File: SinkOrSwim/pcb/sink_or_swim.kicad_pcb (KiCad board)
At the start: 2 copper layers, 42.7 x 68.1 mm, 23 parts, among them P101 CONN_01X02, P102 CONN_01X03, P103 CONN_01X02, P201 CONN_01X01, Q201 BUK9575-100A, U201 LMV358, U401 LM2931

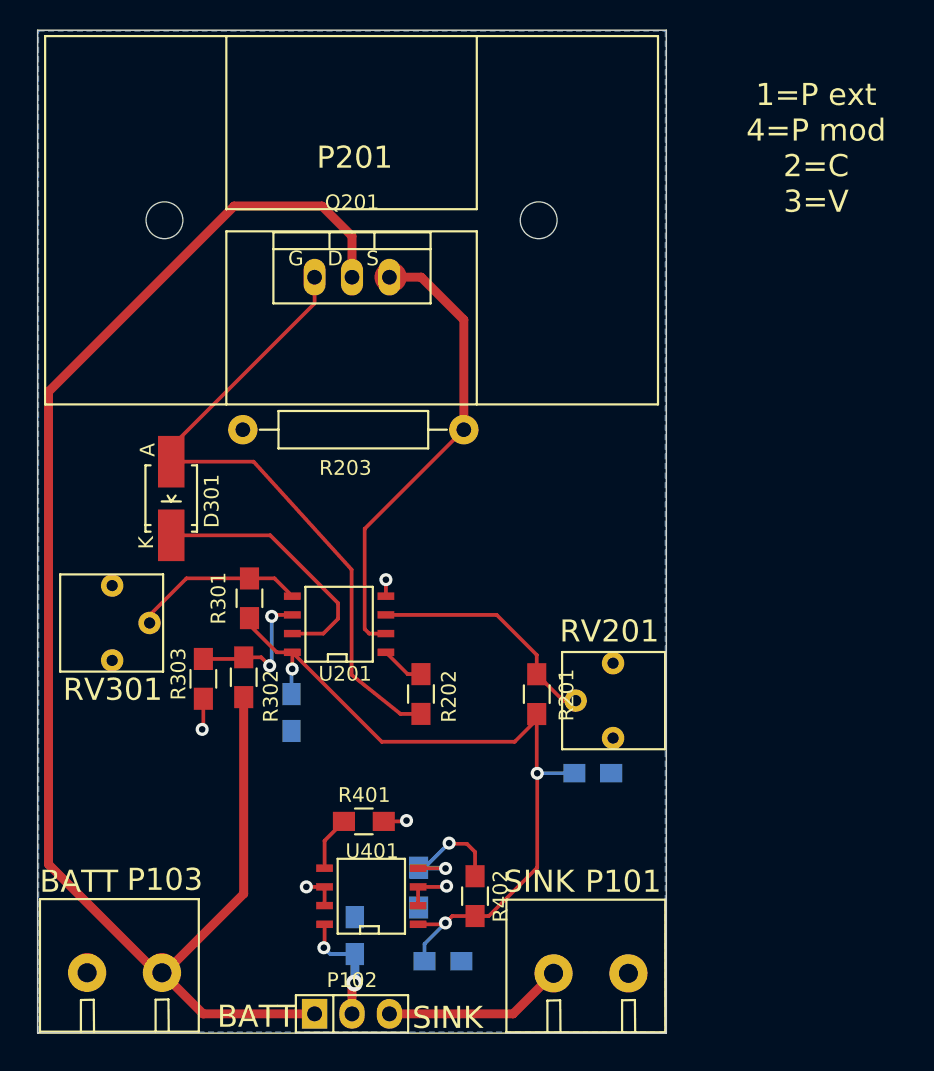
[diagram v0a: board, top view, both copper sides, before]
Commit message: Better Layout.  Added 2 1x2 pin headers to be able to test current.
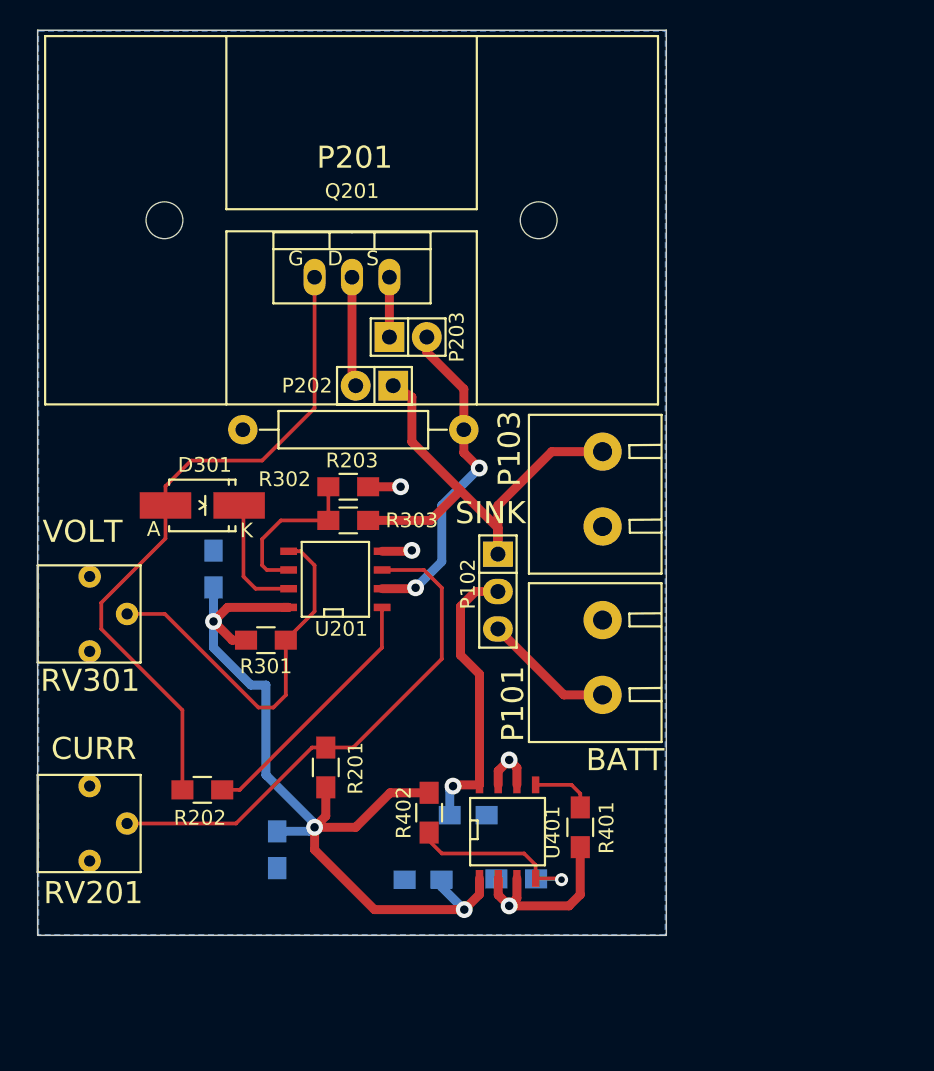
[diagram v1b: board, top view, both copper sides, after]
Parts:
- added P202: B4_FET, Pin_Headers:Pin_Header_Straight_1x02, F.Cu at (172.2, 91.7)
- added P203: AFTR_FET, Pin_Headers:Pin_Header_Straight_1x02, F.Cu at (174.5, 88.4)
- moved P103 45.5 mm to (187.2, 99.1), turned to 90 degrees
- moved RV201 42.6 mm to (149.4, 118.1), turned to 270 degrees
- moved P102 30.3 mm to (180.6, 105.7), turned to 270 degrees
- moved C201 22.0 mm to (165.6, 123.2), turned to 270 degrees
- moved P101 20.6 mm to (187.2, 110.5), turned to 90 degrees
- moved R303 16.3 mm to (170.4, 98.6), turned to 0 degrees
- moved R202 16.2 mm to (160.5, 119.1), turned to 0 degrees
- moved R201 15.2 mm to (168.9, 117.6)
- moved R401 14.7 mm to (186.2, 121.7), turned to 270 degrees
- moved R302 12.8 mm to (170.4, 100.8), turned to 180 degrees
- moved C401 11.2 mm to (178.6, 120.8), turned to 0 degrees
- moved C301 11.1 mm to (161.3, 104.1), turned to 90 degrees
- moved U401 10.2 mm to (181.2, 122.0), turned to 0 degrees
- moved R403 6.65 mm to (181.8, 125.2), turned to 180 degrees
- moved R402 6.46 mm to (175.9, 120.7), turned to 90 degrees
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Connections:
- Q201 pad S: Net-(Q201-PadS) -> GND
- R203 pad 1: Net-(Q201-PadS) -> GND
- U201 pad 2: Net-(Q201-PadS) -> GND
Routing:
- net /CurrentControl/Current_Sink+: track 105.3 -> 41.4 mm
- net GND: track 10.9 -> 47.4 mm, vias 5 -> 6
- net Net-(Q201-PadS): track 31.8 -> 0.00 mm
- net Net-(R201-Pad2): track 16.1 -> 35.4 mm
- net Net-(R202-Pad2): track 2.99 -> 17.6 mm
- net Net-(R301-Pad2): track 11.8 -> 26.1 mm
- net /Power Regulation/Vin: track 8.02 -> 19.5 mm, vias 2 -> 1
- net Net-(D301-Pad2): track 17.8 -> 8.35 mm
- net 2.7V: track 52.9 -> 61.7 mm
- net Net-(P101-Pad1): track 12.3 -> 8.96 mm
- net Net-(R302-Pad2): track 9.63 -> 11.0 mm, vias 2 -> 0
- net /CurrentControl/FET_Gate: track 44.8 -> 45.9 mm
- net Net-(R402-Pad1): track 12.0 -> 12.9 mm, vias 2 -> 1
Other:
- board size 42.7 x 68.1 mm -> 42.7 x 61.4 mm
- board text added: "CURR"
- board text added: "VOLT"

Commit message: Testing a tag csos_v1
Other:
- board text added: "Brooke Hedrick"
- board text added: "Current Sink Or Swim v1"

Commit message: Labeling the pcb
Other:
- board text added: "Creative Commons: CC-BY 02.21.2015"
- board text added: "SinkOrSwim : csos_v1"
- board text added: "brooke.t.hedick@gmail.com"
- board text added: "https://github.com/hedrickbt/ContextualElectronics.git"
- board text removed: "Current Sink Or Swim v1"
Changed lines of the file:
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@@
     (area 148.797 67.513999 200.548 129.050001)
     (thickness 1.6)
-    (drawings 11)
+    (drawings 14)
     (tracks 141)
     (zones 0)
@@
     )
   )
-  (gr_text "Current Sink Or Swim v1" (at 164.338 71.628 180) (layer B.SilkS)
+  (gr_text "Creative Commons: CC-BY\n02.21.2015\n\n" (at 153.162 73.152 90) (layer B.SilkS)
+    (effects (font (size 1.5 1.5) (thickness 0.3)) (justify left mirror))
+  )
+  (gr_text brooke.t.hedick@gmail.com (at 165.1 69.342 180) (layer B.SilkS)
     (effects (font (size 1.5 1.5) (thickness 0.3)) (justify mirror))
   )
-  (gr_text "Brooke Hedrick" (at 158.75 69.342 180) (layer B.SilkS)
+  (gr_text "SinkOrSwim : csos_v1" (at 188.722 80.772 90) (layer B.SilkS)
     (effects (font (size 1.5 1.5) (thickness 0.3)) (justify mirror))
   )
+  (gr_text https://github.com/hedrickbt/ContextualElectronics.git (at 190.5 84.328 90) (layer B.SilkS)
+    (effects (font (size 0.75 0.75) (thickness 0.1)) (justify mirror))
+  )
+  (gr_text "Brooke Hedrick" (at 158.496 71.374 180) (layer B.SilkS)
+    (effects (font (size 1.5 1.5) (thickness 0.3)) (justify mirror))
+  )
